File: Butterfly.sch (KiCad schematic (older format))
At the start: 1 part

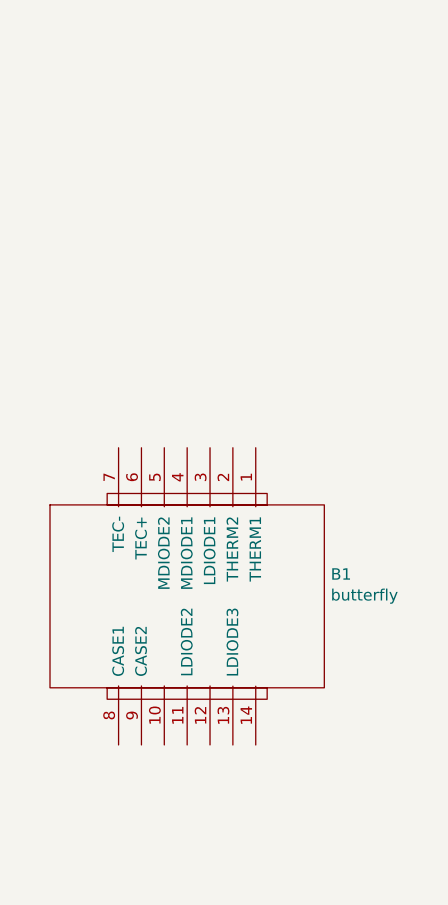
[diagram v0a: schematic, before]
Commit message: TEC on butterfly
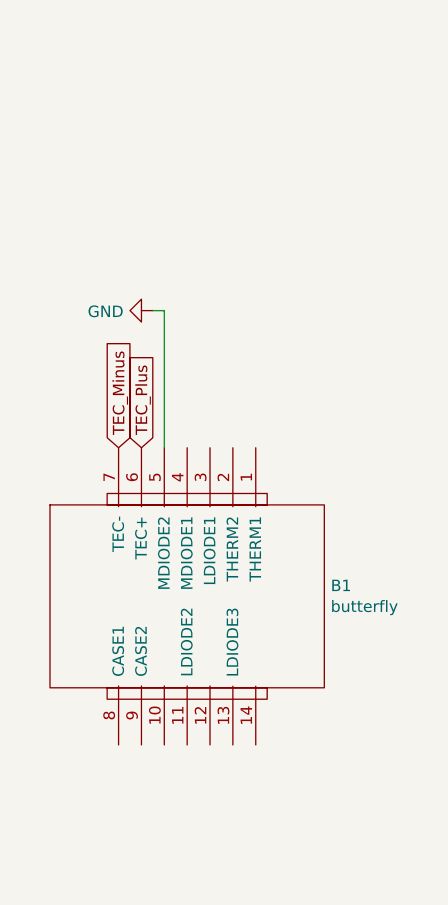
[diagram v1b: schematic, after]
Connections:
- net GND: now reaches B1.5 (MDIODE2)
- net TEC_Plus: now reaches B1.6 (TEC+)
- net TEC_Minus: now reaches B1.7 (TEC-)
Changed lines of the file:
@@
 Comment4 ""
 $EndDescr
+Text GLabel 5550 3200 1    50   Input ~ 0
+TEC_Plus
 $Comp
 L New_Library_for_first_symbol:butterfly B1
-U 1 1 60DE129D
+U 1 1 60DEB546
 P 5750 3850
-F 0 "B1" H 6378 3946 50  0000 L CNN
-F 1 "butterfly" H 6378 3855 50  0000 L CNN
+F 0 "B1" H 6378 3896 50  0000 L CNN
+F 1 "butterfly" H 6378 3805 50  0000 L CNN
 F 2 "" H 5750 3850 50  0001 C CNN
 F 3 "" H 5750 3850 50  0001 C CNN
@@
 	1    0    0    -1
 $EndComp
+Text GLabel 5450 3200 1    50   Input ~ 0
+TEC_Minus
+$Comp
+L power:GND #PWR?
+U 1 1 60DED473
+P 5600 2600
+F 0 "#PWR?" H 5600 2350 50  0001 C CNN
+F 1 "GND" V 5605 2472 50  0000 R CNN
+F 2 "" H 5600 2600 50  0001 C CNN
+F 3 "" H 5600 2600 50  0001 C CNN
+	1    5600 2600
+	0    1    1    0
+$EndComp
+Wire Wire Line
+	5650 3200 5650 2600
+Wire Wire Line
+	5650 2600 5600 2600
 $EndSCHEMATC

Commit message: finish monitor on butterfly
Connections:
- net Monitor+_To_AIN2: now reaches B1.4 (MDIODE1)
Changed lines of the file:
@@
 Wire Wire Line
 	5650 2600 5600 2600
+Text GLabel 5750 3200 1    50   Input ~ 0
+Monitor+_To_AIN2
 $EndSCHEMATC

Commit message: FINISH Butterfly for QA
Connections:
- net GND: now also B1.2 (THERM2), B1.8 (CASE1), B1.9 (CASE2)
- net Butterfly_Thermistor: now reaches B1.1 (THERM1)
- net LASER_3.3V: now reaches B1.11 (LDIODE2)
- net LASER_V-: now reaches B1.3 (LDIODE1)
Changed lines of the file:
@@
 Text GLabel 5750 3200 1    50   Input ~ 0
 Monitor+_To_AIN2
+Text GLabel 5750 4500 3    50   Input ~ 0
+LASER_3.3V
+Text GLabel 5850 3200 1    50   Input ~ 0
+LASER_V-
+Text GLabel 6050 3200 1    50   Input ~ 0
+Butterfly_Thermistor
+Wire Wire Line
+	5950 3200 5950 2400
+Wire Wire Line
+	5950 2400 5600 2400
+Wire Wire Line
+	5600 2400 5600 2600
+Connection ~ 5600 2600
+Wire Wire Line
+	5550 4500 5450 4500
+Connection ~ 5450 4500
+Wire Wire Line
+	5450 4500 5400 4500
+$Comp
+L power:GND #PWR?
+U 1 1 60E00331
+P 5400 4500
+F 0 "#PWR?" H 5400 4250 50  0001 C CNN
+F 1 "GND" V 5405 4372 50  0000 R CNN
+F 2 "" H 5400 4500 50  0001 C CNN
+F 3 "" H 5400 4500 50  0001 C CNN
+	1    5400 4500
+	0    1    1    0
+$EndComp
 $EndSCHEMATC

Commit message: assigned butterfly footprint
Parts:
- B1: footprint (none) -> footprint libraries:Butterfly
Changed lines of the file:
@@
 F 0 "B1" H 6378 3896 50  0000 L CNN
 F 1 "butterfly" H 6378 3805 50  0000 L CNN
-F 2 "" H 5750 3850 50  0001 C CNN
+F 2 "footprint libraries:Butterfly" H 5750 3850 50  0001 C CNN
 F 3 "" H 5750 3850 50  0001 C CNN
 	1    5750 3850
@@
 TEC_Minus
 $Comp
-L power:GND #PWR?
+L power:GND #PWR0102
 U 1 1 60DED473
 P 5600 2600
-F 0 "#PWR?" H 5600 2350 50  0001 C CNN
+F 0 "#PWR0102" H 5600 2350 50  0001 C CNN
 F 1 "GND" V 5605 2472 50  0000 R CNN
 F 2 "" H 5600 2600 50  0001 C CNN
@@
 	5450 4500 5400 4500
 $Comp
-L power:GND #PWR?
+L power:GND #PWR0103
 U 1 1 60E00331
 P 5400 4500
-F 0 "#PWR?" H 5400 4250 50  0001 C CNN
+F 0 "#PWR0103" H 5400 4250 50  0001 C CNN
 F 1 "GND" V 5405 4372 50  0000 R CNN
 F 2 "" H 5400 4500 50  0001 C CNN

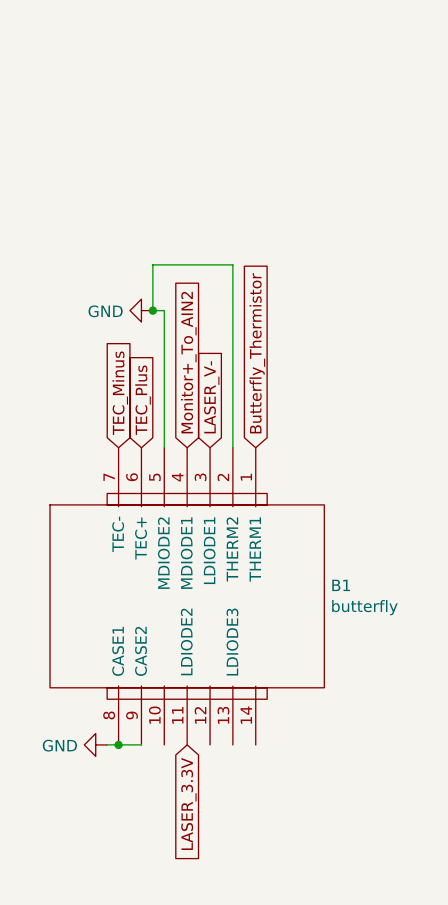
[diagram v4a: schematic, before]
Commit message: added one reisistor to monitor pin
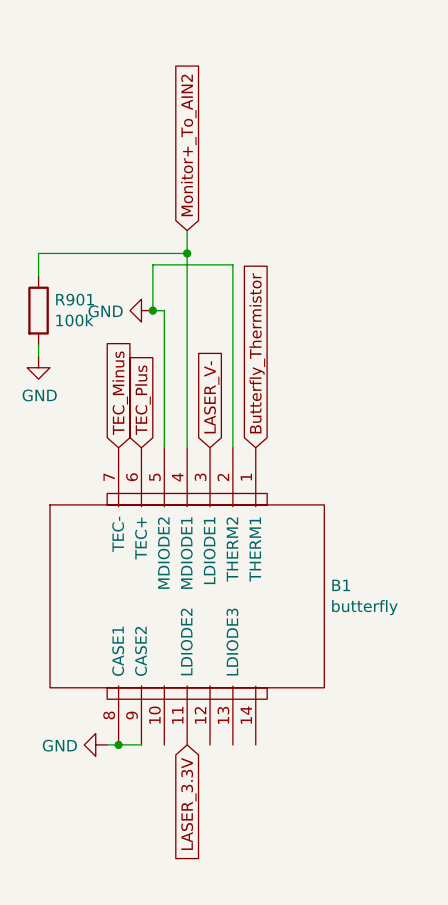
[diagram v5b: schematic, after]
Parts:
- added R901: 100k, Resistor_SMD:R_0402_1005Metric, symbol Device:R
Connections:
- net GND: now also R901.2
- net Monitor+_To_AIN2: now also R901.1
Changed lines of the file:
@@
 Wire Wire Line
 	5650 2600 5600 2600
-Text GLabel 5750 3200 1    50   Input ~ 0
+Text GLabel 5750 2250 1    50   Input ~ 0
 Monitor+_To_AIN2
 Text GLabel 5750 4500 3    50   Input ~ 0
@@
 	0    1    1    0
 $EndComp
+Wire Wire Line
+	5750 3200 5750 2350
+Wire Wire Line
+	5750 2350 5100 2350
+Wire Wire Line
+	5100 2350 5100 2450
+Connection ~ 5750 2350
+Wire Wire Line
+	5750 2350 5750 2250
+$Comp
+L Device:R R901
+U 1 1 60D2C1DF
+P 5100 2600
+F 0 "R901" H 5170 2646 50  0000 L CNN
+F 1 "100k" H 5170 2555 50  0000 L CNN
+F 2 "Resistor_SMD:R_0402_1005Metric" V 5030 2600 50  0001 C CNN
+F 3 "~" H 5100 2600 50  0001 C CNN
+	1    5100 2600
+	1    0    0    -1
+$EndComp
+Wire Wire Line
+	5100 2750 5100 2800
+$Comp
+L power:GND #PWR0104
+U 1 1 60D2CBDA
+P 5100 2800
+F 0 "#PWR0104" H 5100 2550 50  0001 C CNN
+F 1 "GND" H 5105 2627 50  0000 C CNN
+F 2 "" H 5100 2800 50  0001 C CNN
+F 3 "" H 5100 2800 50  0001 C CNN
+	1    5100 2800
+	1    0    0    -1
+$EndComp
 $EndSCHEMATC

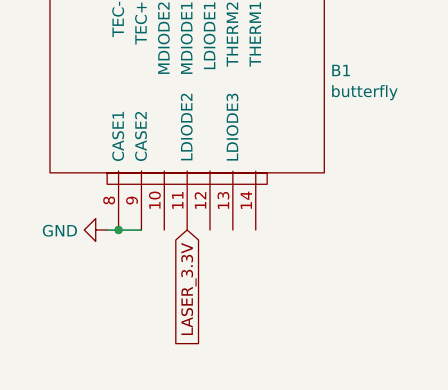
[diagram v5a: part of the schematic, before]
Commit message: QA 7/13 added new usb, made pads smaller, qa'd everything except current control, arduino and thermal control
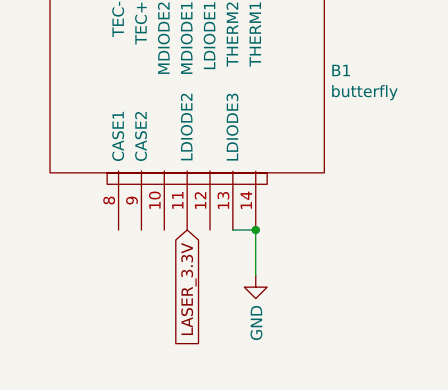
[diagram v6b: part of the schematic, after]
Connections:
- net GND: now also B1.13 (LDIODE3), B1.14; no longer B1.8 (CASE1), B1.9 (CASE2)
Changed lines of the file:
@@
 Text GLabel 5550 3200 1    50   Input ~ 0
 TEC_Plus
-$Comp
-L New_Library_for_first_symbol:butterfly B1
-U 1 1 60DEB546
-P 5750 3850
-F 0 "B1" H 6378 3896 50  0000 L CNN
-F 1 "butterfly" H 6378 3805 50  0000 L CNN
-F 2 "footprint libraries:Butterfly" H 5750 3850 50  0001 C CNN
-F 3 "" H 5750 3850 50  0001 C CNN
-	1    5750 3850
-	1    0    0    -1
-$EndComp
 Text GLabel 5450 3200 1    50   Input ~ 0
 TEC_Minus
@@
 Connection ~ 5600 2600
 Wire Wire Line
-	5550 4500 5450 4500
-Connection ~ 5450 4500
-Wire Wire Line
-	5450 4500 5400 4500
-$Comp
-L power:GND #PWR0103
-U 1 1 60E00331
-P 5400 4500
-F 0 "#PWR0103" H 5400 4250 50  0001 C CNN
-F 1 "GND" V 5405 4372 50  0000 R CNN
-F 2 "" H 5400 4500 50  0001 C CNN
-F 3 "" H 5400 4500 50  0001 C CNN
-	1    5400 4500
-	0    1    1    0
-$EndComp
-Wire Wire Line
 	5750 3200 5750 2350
 Wire Wire Line
@@
 	1    0    0    -1
 $EndComp
+$Comp
+L power:GND #PWR0103
+U 1 1 60E00331
+P 6050 4700
+F 0 "#PWR0103" H 6050 4450 50  0001 C CNN
+F 1 "GND" V 6055 4572 50  0000 R CNN
+F 2 "" H 6050 4700 50  0001 C CNN
+F 3 "" H 6050 4700 50  0001 C CNN
+	1    6050 4700
+	1    0    0    -1
+$EndComp
+$Comp
+L New_Library_for_first_symbol:butterfly B1
+U 1 1 60DEB546
+P 5750 3850
+F 0 "B1" H 6378 3896 50  0000 L CNN
+F 1 "butterfly" H 6378 3805 50  0000 L CNN
+F 2 "footprint libraries:Butterfly" H 5750 3850 50  0001 C CNN
+F 3 "" H 5750 3850 50  0001 C CNN
+	1    5750 3850
+	1    0    0    -1
+$EndComp
+Wire Wire Line
+	6050 4700 6050 4500
+Wire Wire Line
+	5950 4500 6050 4500
+Connection ~ 6050 4500
 $EndSCHEMATC
